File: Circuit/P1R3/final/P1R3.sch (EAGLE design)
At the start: 88 parts, among them J1 MICRO_USB_B_HIROSE_ZX62R-B-5P, U1 MK20DX256VLH7, U2 TPS61200, U3 MPU-9250, Y1 32.768KHz, Y2 16Mhz/8pF, Y3 26 Mhz, Y4 16 Mhz

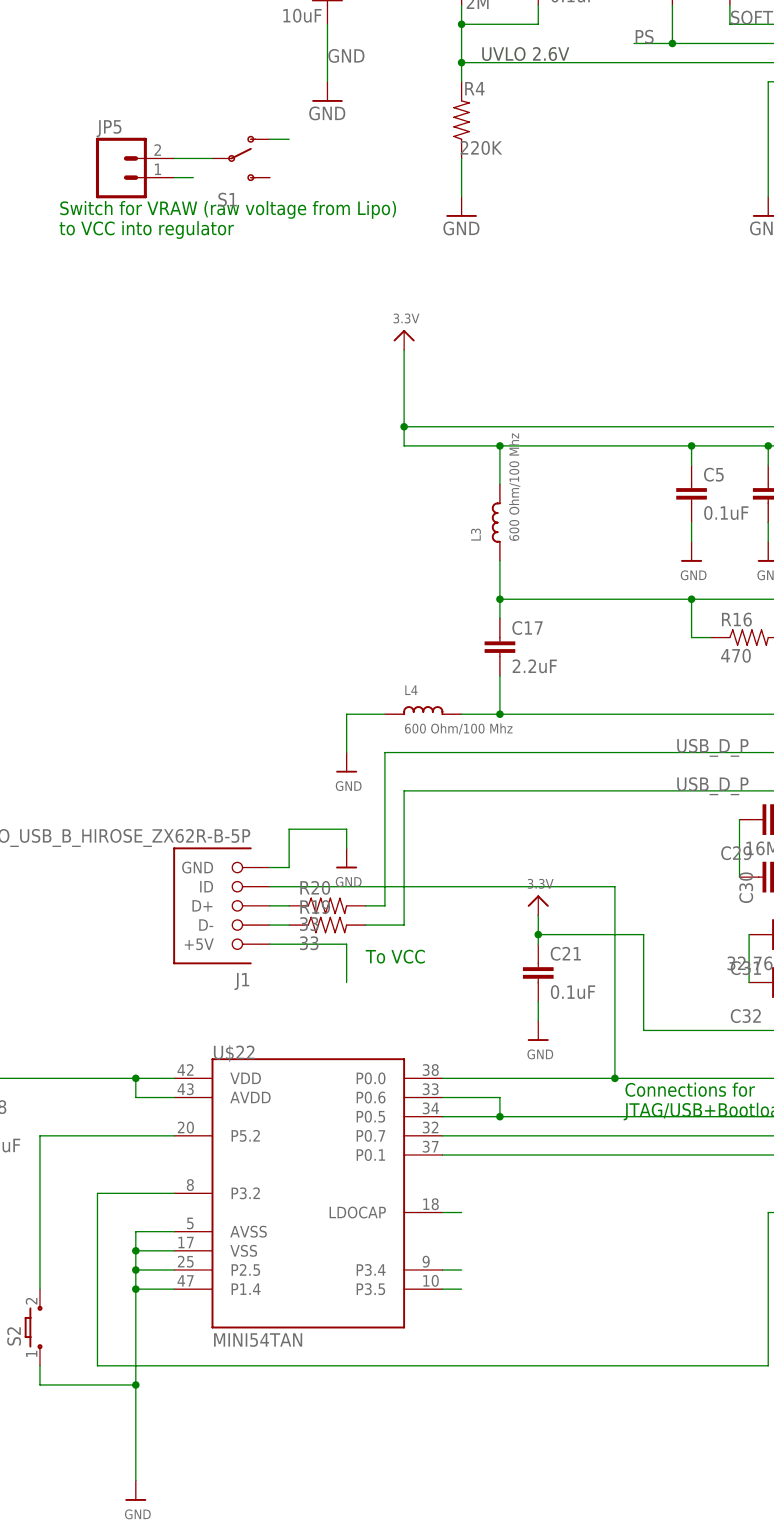
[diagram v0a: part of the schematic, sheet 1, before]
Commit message: Added four from LED drivers to R4. Corrected R3 bootloader circuit. Rerouted switch in schematic and board on both R3 and R4 for proper isolation of USB and lipo voltage. Ready for final review
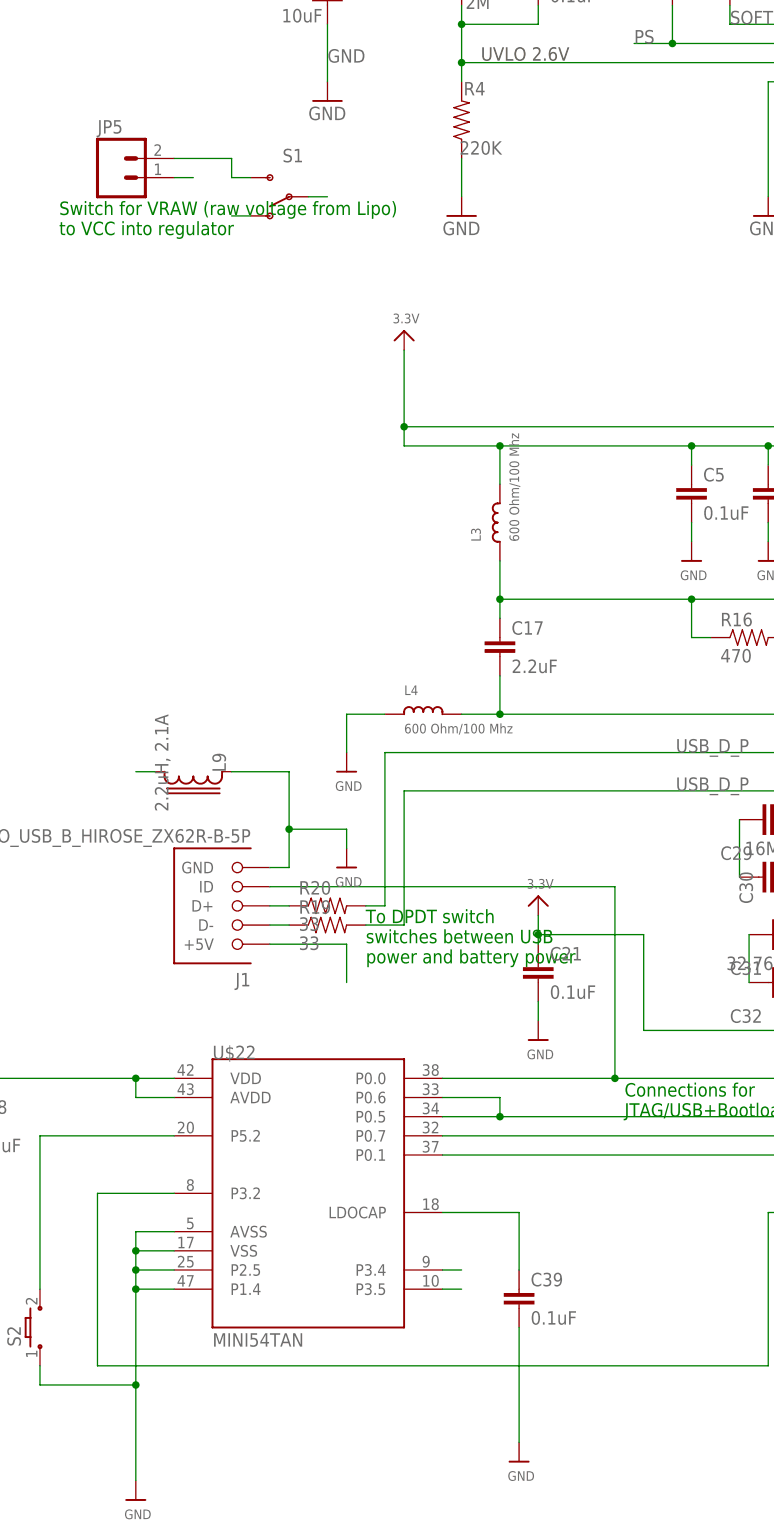
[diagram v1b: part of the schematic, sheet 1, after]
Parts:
- added C39: 0.1uF, appfruits:CAPACITOR-0.1UF
- added L9: 2.2uH, 2.1A, appfruits:LPS30152.2UH
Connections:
- removed net VRAW: JP5.2, S1.P
- new net N$40: L9.2
- new net VBAT: JP5.2, S1.S
- new net VUSB: J1.+5V, S1.O
- net GND: now also C39.2, L9.1
- net N$49: now also C39.1
- net VCC: now also S1.P; no longer J1.+5V, S1.O
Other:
- note added: "To DPDT switch switches between USB power and battery power"
- note removed: "To VCC"
- moved on the sheet: S1
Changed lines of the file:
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@@
 </class>
 <class number="2" name="Top GND Pour" width="0" drill="0">
+<clearance class="0" value="0.127"/>
+<clearance class="1" value="1.27"/>
 </class>
 </classes>
@@
 <part name="R19" library="SparkFun" deviceset="RESISTOR" device="0402-RES" value="33"/>
 <part name="R20" library="SparkFun" deviceset="RESISTOR" device="0402-RES" value="33"/>
+<part name="C39" library="appfruits" deviceset="CAPACITOR" device="-0.1UF" value="0.1uF"/>
+<part name="U$13" library="microbuilder" deviceset="GND" device=""/>
+<part name="L9" library="appfruits" deviceset="LPS3015" device="2.2UH" value="2.2uH, 2.1A"/>
 </parts>
 <sheets>
@@
 <text x="120.65" y="-121.92" size="1.778" layer="91">RTC</text>
 <text x="264.16" y="-172.72" size="1.778" layer="91">3.3V Breakout</text>
-<text x="50.8" y="-121.92" size="1.778" layer="91">To VCC</text>
+<text x="50.8" y="-121.92" size="1.778" layer="91">To DPDT switch
+switches between USB
+power and battery power</text>
 </plain>
 <instances>
@@
 <instance part="GND1" gate="1" x="226.06" y="-22.86"/>
 <instance part="JP5" gate="G$1" x="17.78" y="-17.78"/>
-<instance part="S1" gate="1" x="33.02" y="-15.24"/>
+<instance part="S1" gate="1" x="40.64" y="-20.32" rot="R180"/>
 <instance part="R8" gate="G$1" x="254" y="-60.96"/>
 <instance part="LED2" gate="G$1" x="264.16" y="-60.96" rot="R90"/>
@@
 <instance part="R19" gate="G$1" x="45.72" y="-116.84"/>
 <instance part="R20" gate="G$1" x="45.72" y="-114.3"/>
+<instance part="C39" gate="G$1" x="71.12" y="-167.64"/>
+<instance part="U$13" gate="G$1" x="71.12" y="-187.96"/>
+<instance part="L9" gate="G$1" x="27.94" y="-96.52" smashed="yes" rot="R180">
+<attribute name="NAME" x="30.48" y="-93.98" size="1.778" layer="95" rot="R270"/>
+<attribute name="VALUE" x="22.86" y="-88.9" size="1.778" layer="96" rot="R270"/>
+</instance>
 </instances>
 <busses>
@@
 <wire x1="48.26" y1="-104.14" x2="48.26" y2="-106.68" width="0.1524" layer="91"/>
 <pinref part="U$11" gate="G$1" pin="GND"/>
+<pinref part="L9" gate="G$1" pin="1"/>
+<wire x1="33.02" y1="-96.52" x2="40.64" y2="-96.52" width="0.1524" layer="91"/>
+<wire x1="40.64" y1="-96.52" x2="40.64" y2="-104.14" width="0.1524" layer="91"/>
+<junction x="40.64" y="-104.14"/>
+</segment>
+<segment>
+<pinref part="C39" gate="G$1" pin="2"/>
+<wire x1="71.12" y1="-170.18" x2="71.12" y2="-185.42" width="0.1524" layer="91"/>
+<pinref part="U$13" gate="G$1" pin="GND"/>
 </segment>
 </net>
@@
 </segment>
 <segment>
-<pinref part="S1" gate="1" pin="O"/>
-<wire x1="38.1" y1="-12.7" x2="40.64" y2="-12.7" width="0.1524" layer="91"/>
-</segment>
-<segment>
-<pinref part="J1" gate="G$1" pin="+5V"/>
-<wire x1="38.1" y1="-119.38" x2="48.26" y2="-119.38" width="0.1524" layer="91"/>
-<wire x1="48.26" y1="-119.38" x2="48.26" y2="-124.46" width="0.1524" layer="91"/>
+<pinref part="S1" gate="1" pin="P"/>
+<wire x1="43.18" y1="-20.32" x2="45.72" y2="-20.32" width="0.1524" layer="91"/>
 </segment>
 </net>
@@
 <pinref part="U1" gate="G$1" pin="ADC0_DM3"/>
 <wire x1="203.2" y1="-121.92" x2="210.82" y2="-121.92" width="0.1524" layer="91"/>
-</segment>
-</net>
-<net name="VRAW" class="2">
-<segment>
-<pinref part="JP5" gate="G$1" pin="2"/>
-<pinref part="S1" gate="1" pin="P"/>
-<wire x1="25.4" y1="-15.24" x2="30.48" y2="-15.24" width="0.1524" layer="91"/>
 </segment>
 </net>
@@
 <segment>
 <pinref part="U$22" gate="G$1" pin="LDOCAP"/>
-<wire x1="60.96" y1="-154.94" x2="63.5" y2="-154.94" width="0.1524" layer="91"/>
+<pinref part="C39" gate="G$1" pin="1"/>
+<wire x1="60.96" y1="-154.94" x2="71.12" y2="-154.94" width="0.1524" layer="91"/>
+<wire x1="71.12" y1="-154.94" x2="71.12" y2="-162.56" width="0.1524" layer="91"/>
 </segment>
 </net>
@@
 </segment>
 </net>
+<net name="VUSB" class="0">
+<segment>
+<pinref part="J1" gate="G$1" pin="+5V"/>
+<wire x1="38.1" y1="-119.38" x2="48.26" y2="-119.38" width="0.1524" layer="91"/>
+<wire x1="48.26" y1="-119.38" x2="48.26" y2="-124.46" width="0.1524" layer="91"/>
+</segment>
+<segment>
+<pinref part="S1" gate="1" pin="O"/>
+<wire x1="35.56" y1="-22.86" x2="33.02" y2="-22.86" width="0.1524" layer="91"/>
+</segment>
+</net>
+<net name="VBAT" class="0">
+<segment>
+<pinref part="JP5" gate="G$1" pin="2"/>
+<pinref part="S1" gate="1" pin="S"/>
+<wire x1="35.56" y1="-17.78" x2="33.02" y2="-17.78" width="0.1524" layer="91"/>
+<wire x1="25.4" y1="-15.24" x2="33.02" y2="-15.24" width="0.1524" layer="91"/>
+<wire x1="33.02" y1="-15.24" x2="33.02" y2="-17.78" width="0.1524" layer="91"/>
+</segment>
+</net>
+<net name="N$40" class="0">
+<segment>
+<pinref part="L9" gate="G$1" pin="2"/>
+<wire x1="22.86" y1="-96.52" x2="20.32" y2="-96.52" width="0.1524" layer="91"/>
+</segment>
+</net>
